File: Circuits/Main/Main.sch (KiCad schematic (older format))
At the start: 33 parts, among them CON1 BARREL_JACK, P1 led_stop, P10 toEncoder_MotorL, P11 toEncoder_motorR, P12 conn_resetButton, P13 conn_resetButton, P2 led_droite_face, P3 led_droite_cote, P4 led_gauche_face, P5 led_gauche_cote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

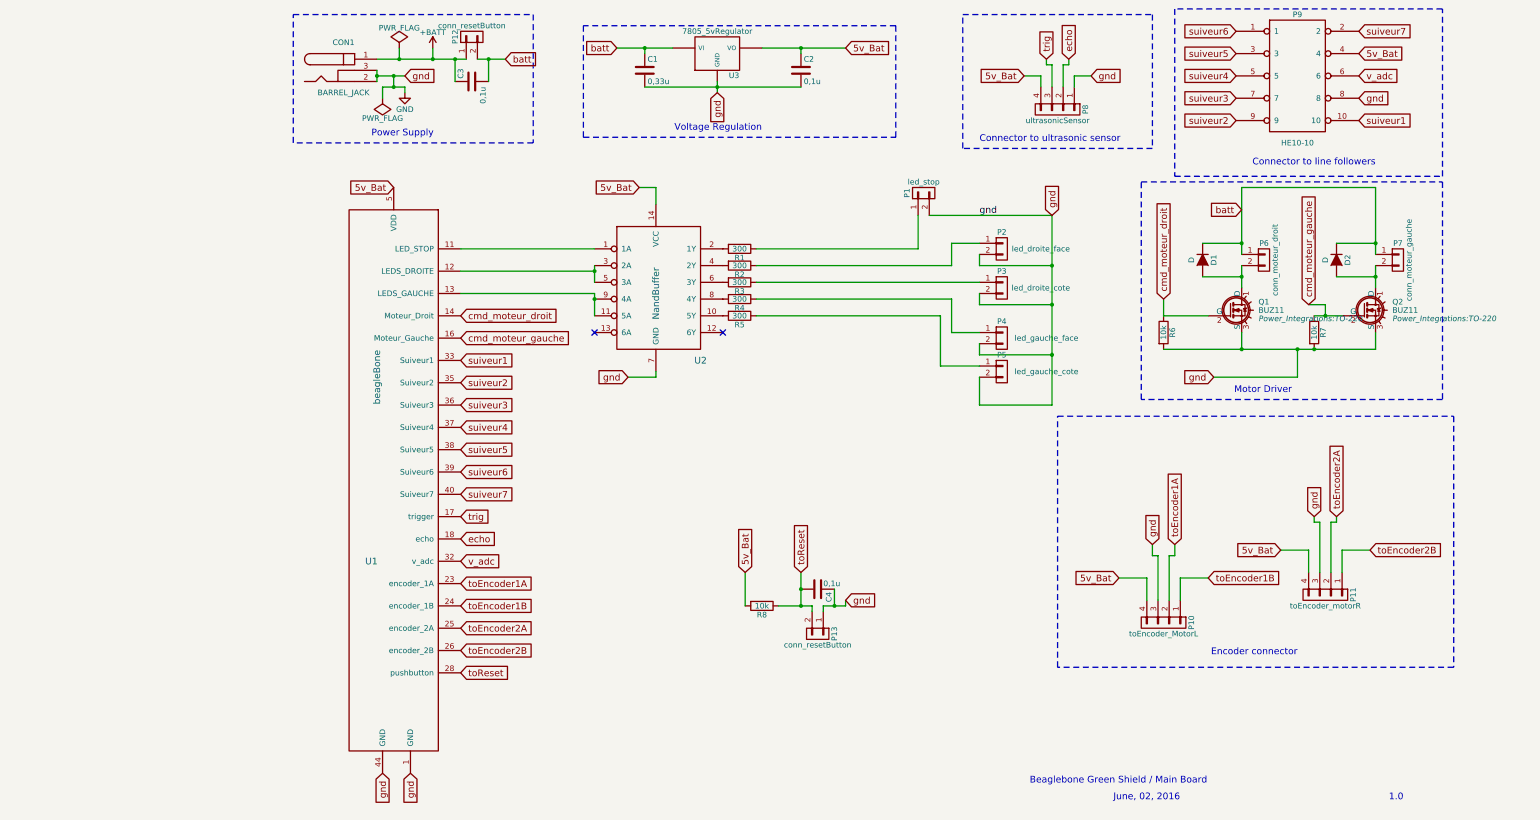
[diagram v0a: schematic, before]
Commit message: Ajout de la carte principale (schemas + gerbers) et intégration
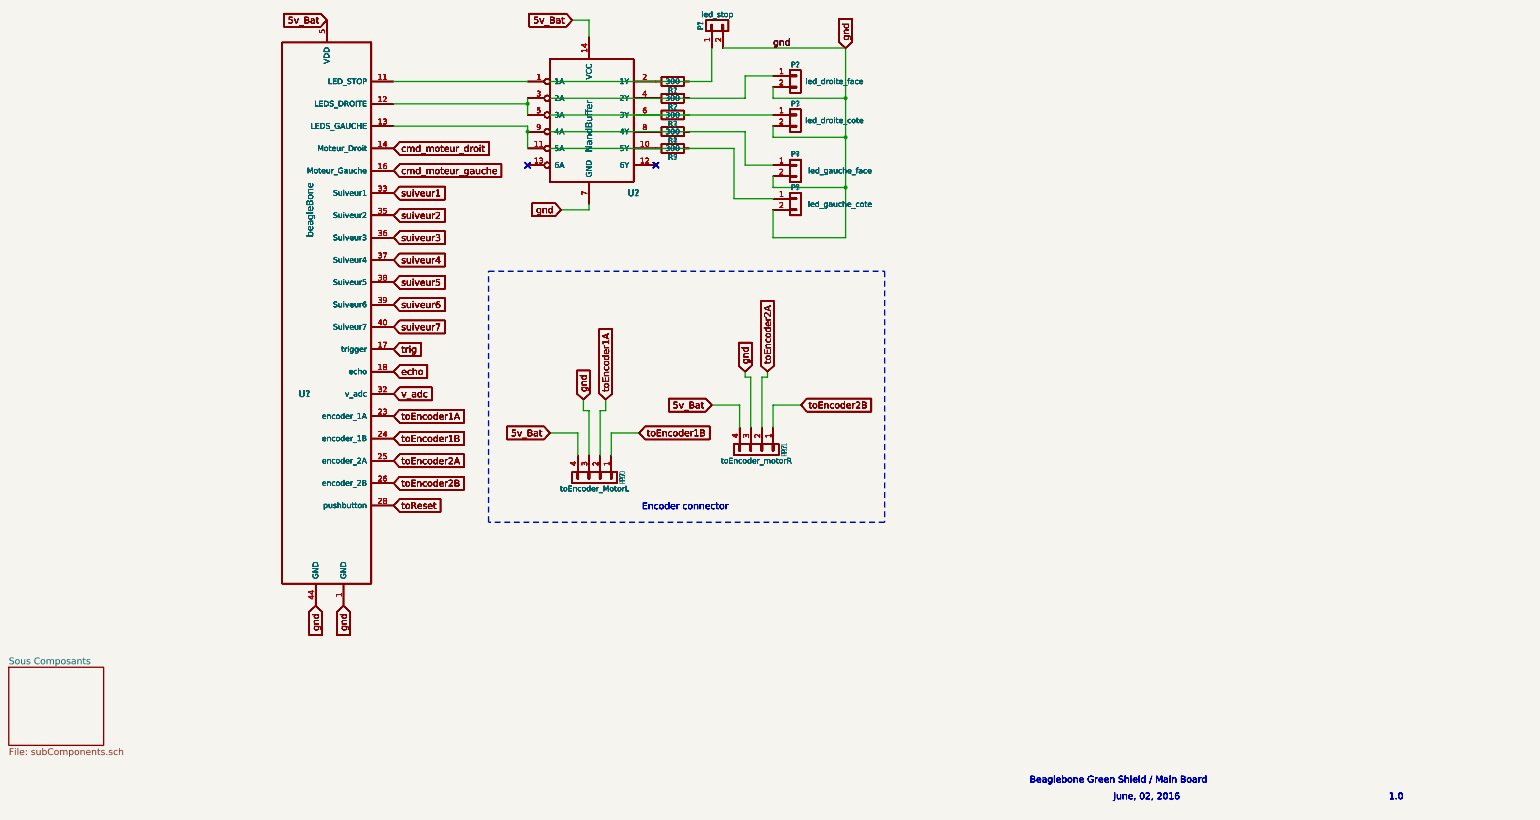
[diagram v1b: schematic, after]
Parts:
- removed C1: 0,33u, Capacitors_ThroughHole:C_Disc_D3_P2.5, symbol C
- removed C2, C3, C4: 0,1u, Capacitors_ThroughHole:C_Disc_D3_P2.5, symbol C
- removed CON1: BARREL_JACK, Connect:BARREL_JACK, symbol BARREL_JACK
- removed D1, D2: D, Diodes_ThroughHole:Diode_DO-35_SOD27_Horizontal_RM10, symbol D
- removed P12, P13: conn_resetButton, Pin_Headers:Pin_Header_Straight_1x02, symbol CONN_01X02
- removed P6: conn_moteur_droit, Pin_Headers:Pin_Header_Straight_1x02, symbol CONN_01X02
- removed P7: conn_moteur_gauche, Pin_Headers:Pin_Header_Straight_1x02, symbol CONN_01X02
- removed P8: ultrasonicSensor, Pin_Headers:Pin_Header_Straight_1x04, symbol CONN_01X04
- removed P9: HE10-10, Connect:he10-10d, symbol HE10-10
- removed Q1, Q2: BUZ11, Power_Integrations:TO-220, symbol BUZ11
- removed R6, R7, R8: 10k, Resistors_ThroughHole:Resistor_Horizontal_RM10mm, symbol R
- removed U3: 7805_5vRegulator, MES_EMPREINTES:voltageRegulator5v, symbol 7805_5vRegulator
- added P? (x3): led_stop, Pin_Headers:Pin_Header_Straight_1x02, symbol CONN_01X02
- added P? (x3): led_gauche_cote, Pin_Headers:Pin_Header_Straight_1x02, symbol CONN_01X02
- added P? (x3): led_gauche_face, Pin_Headers:Pin_Header_Straight_1x02, symbol CONN_01X02
- added P? (x3): led_droite_face, Pin_Headers:Pin_Header_Straight_1x02, symbol CONN_01X02
- added P? (x3): led_droite_cote, Pin_Headers:Pin_Header_Straight_1x02, symbol CONN_01X02
- added P? (x3): toEncoder_MotorL, Pin_Headers:Pin_Header_Straight_1x04, symbol CONN_01X04
- added P? (x3): toEncoder_motorR, Pin_Headers:Pin_Header_Straight_1x04, symbol CONN_01X04
- added R? (x15): 300, Resistors_ThroughHole:Resistor_Horizontal_RM10mm, symbol R
- added U? (x3): NandBuffer, MES_EMPREINTES:NandBuffer, symbol NandBuffer
- added U? (x3): beagleBone, MES_EMPREINTES:beagleBoneGRNFootPrint, symbol beagleBone
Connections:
- net labels removed: +BATT, GND, batt
- wire segments 106 -> 51
- no-connect marks 2 -> 8
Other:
- note removed: "Connector to line followers"
- note removed: "Connector to ultrasonic sensor"
- note removed: "Motor Driver"
- note removed: "Power Supply"
- note removed: "Voltage Regulation"
- moved on the sheet: P1, P10, P11, P2, P3, P4, P5, R1, R2, R3, R4, R5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

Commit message: Ameliorations cartes + rapport
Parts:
- removed P10, P? (x2): toEncoder_MotorL, Pin_Headers:Pin_Header_Straight_1x04, symbol CONN_01X04
- removed P? (x3): led_stop, Pin_Headers:Pin_Header_Straight_1x02, symbol CONN_01X02
- removed P? (x3): led_gauche_cote, Pin_Headers:Pin_Header_Straight_1x02, symbol CONN_01X02
- removed P? (x3): led_gauche_face, Pin_Headers:Pin_Header_Straight_1x02, symbol CONN_01X02
- removed P? (x3): led_droite_face, Pin_Headers:Pin_Header_Straight_1x02, symbol CONN_01X02
- removed P? (x3): led_droite_cote, Pin_Headers:Pin_Header_Straight_1x02, symbol CONN_01X02
- removed P? (x3): toEncoder_motorR, Pin_Headers:Pin_Header_Straight_1x04, symbol CONN_01X04
- removed R? (x15): 300, Resistors_ThroughHole:Resistor_Horizontal_RM10mm, symbol R
- removed U? (x3): NandBuffer, MES_EMPREINTES:NandBuffer, symbol NandBuffer
- removed U? (x3): beagleBone, MES_EMPREINTES:beagleBoneGRNFootPrint, symbol beagleBone
- gave numbers to parts that had none: 1
- renumbered P1 to P2, P11 to P3, P2 to P4, P3 to P5, P4 to P6, P5 to P7
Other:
- note removed: "1.0"
- note removed: "Beaglebone Green Shield / Main Board"
- note removed: "June, 02, 2016"
